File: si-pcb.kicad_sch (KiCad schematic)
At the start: 131 parts

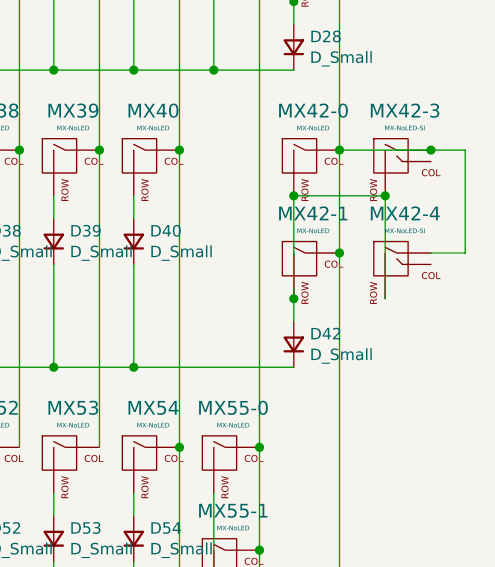
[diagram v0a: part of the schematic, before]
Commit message: Edit BEA switch symbols
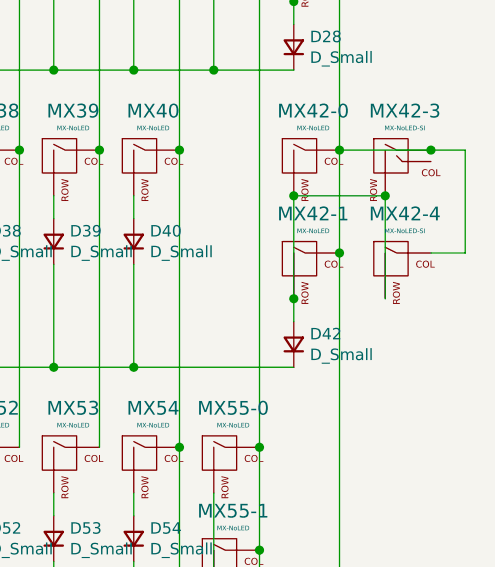
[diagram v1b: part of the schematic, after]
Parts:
- MX42-4: footprint hitek725:Hitek725-BigAssEnter-separated-pins-reversed -> hitek725:Hitek725-BigAssEnter-reversed; symbol MX_Alps_Hybrid:MX-NoLED-SI -> MX_Alps_Hybrid:MX-NoLED
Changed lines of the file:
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@@
+    (pin "2")
+  )
+  (symbol (lib_id "MX_Alps_Hybrid:MX-NoLED") (at 170.18 113.03 0) (unit 1)
+    (in_bom yes) (on_board yes)
+    (property "Reference" "MX42-4" (id 0) (at 171.0969 107.4292 0)
+      (effects (font (size 1.524 1.524)))
+    )
+    (property "Value" "MX-NoLED-SI" (id 1) (at 171.0969 109.3189 0)
+      (effects (font (size 0.508 0.508)))
+    )
+    (property "Footprint" "hitek725:Hitek725-BigAssEnter-reversed" (id 2) (at 154.305 113.665 0)
+      (effects (font (size 1.524 1.524)) hide)
+    )
+    (property "Datasheet" "" (id 3) (at 154.305 113.665 0)
+      (effects (font (size 1.524 1.524)) hide)
+    )
+    (pin "1")
     (pin "2")
   )
@@
     )
     (property "Datasheet" "" (id 3) (at 154.305 102.235 0)
-      (effects (font (size 1.524 1.524)) hide)
-    )
-    (pin "1")
-    (pin "2")
-    (pin "")
-  )
-  (symbol (lib_id "MX_Alps_Hybrid:MX-NoLED-SI") (at 170.18 113.03 0) (unit 1)
-    (in_bom yes) (on_board yes)
-    (property "Reference" "MX42-4" (id 0) (at 171.0969 107.4292 0)
-      (effects (font (size 1.524 1.524)))
-    )
-    (property "Value" "MX-NoLED-SI" (id 1) (at 171.0969 109.3189 0)
-      (effects (font (size 0.508 0.508)))
-    )
-    (property "Footprint" "hitek725:Hitek725-BigAssEnter-separated-pins-reversed" (id 2) (at 154.305 113.665 0)
-      (effects (font (size 1.524 1.524)) hide)
-    )
-    (property "Datasheet" "" (id 3) (at 154.305 113.665 0)
       (effects (font (size 1.524 1.524)) hide)
     )
@@
     )
     (path "/dbc64475-49aa-498c-8392-74ac49997f7c"
-      (reference "MX42-4") (unit 1) (value "MX-NoLED-SI") (footprint "hitek725:Hitek725-BigAssEnter-separated-pins-reversed")
+      (reference "MX42-4") (unit 1) (value "MX-NoLED-SI") (footprint "hitek725:Hitek725-BigAssEnter-reversed")
     )
     (path "/2c6aab79-05c6-4f42-bd7d-b98963fadfff"
